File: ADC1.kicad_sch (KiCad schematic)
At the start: 16 parts, among them U4 ADS112C04

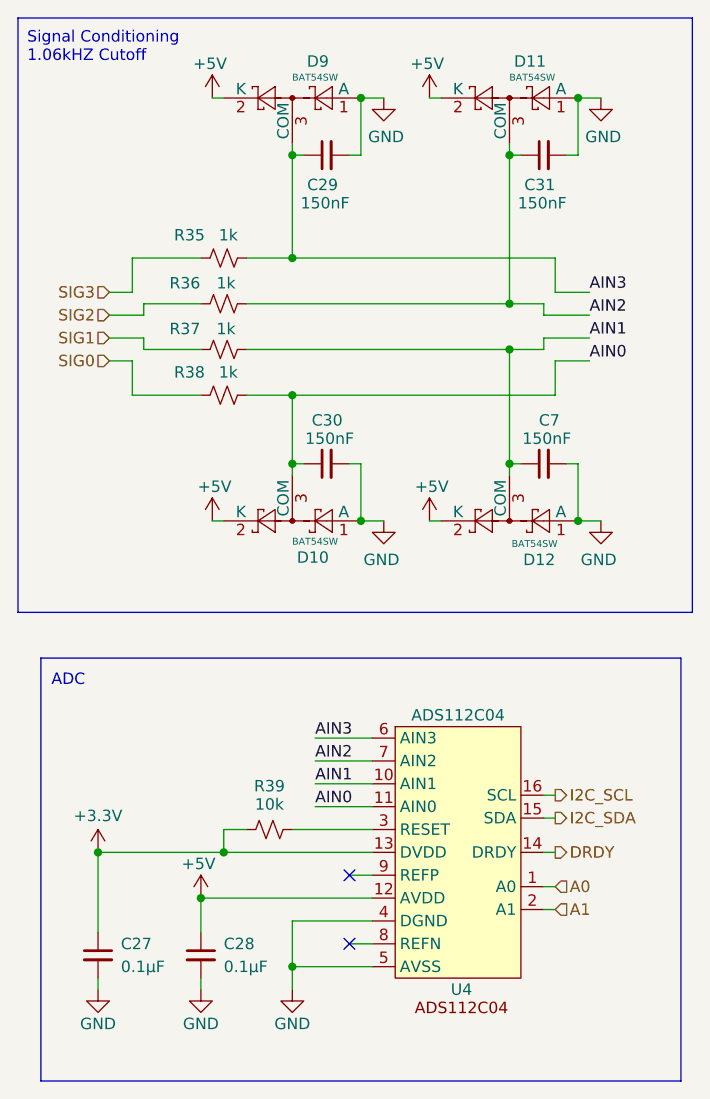
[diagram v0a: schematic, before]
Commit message: Updated to 4-pin fans, moved power pages together, deleted old reference.
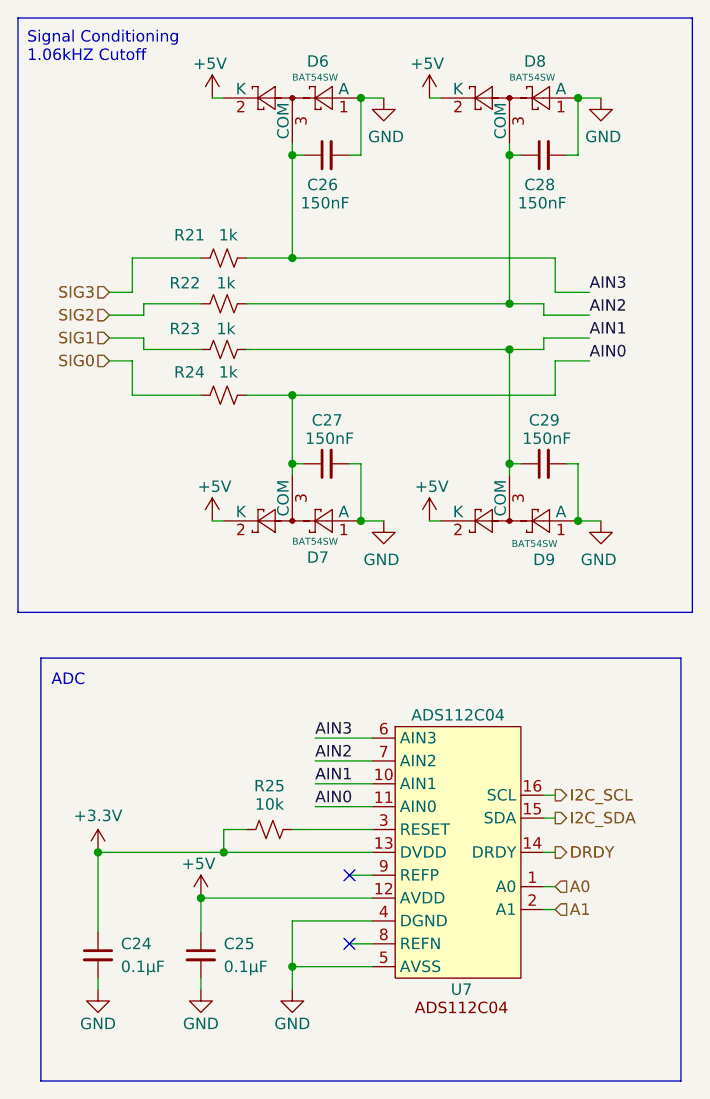
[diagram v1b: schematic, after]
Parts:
- renumbered C27 to C24, C28 to C25, C29 to C26, C30 to C27, C31 to C28, C7 to C29, D9 to D6, D10 to D7, D11 to D8, D12 to D9, R35 to R21, R36 to R22, R37 to R23, R38 to R24, R39 to R25, U4 to U7
